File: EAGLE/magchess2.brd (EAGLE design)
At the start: 49.5 x 40.6 mm, 14 parts

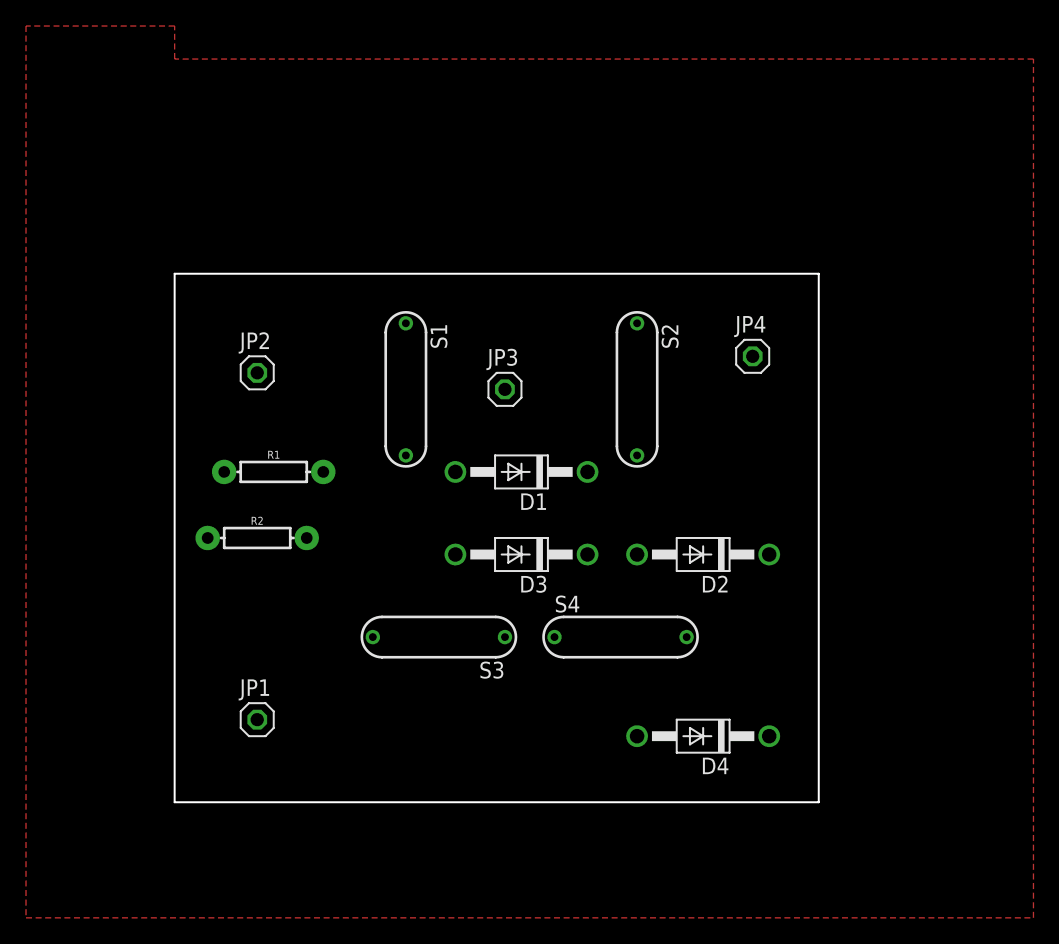
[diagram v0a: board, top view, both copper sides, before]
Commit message: figured out how to work around relaly small garbage
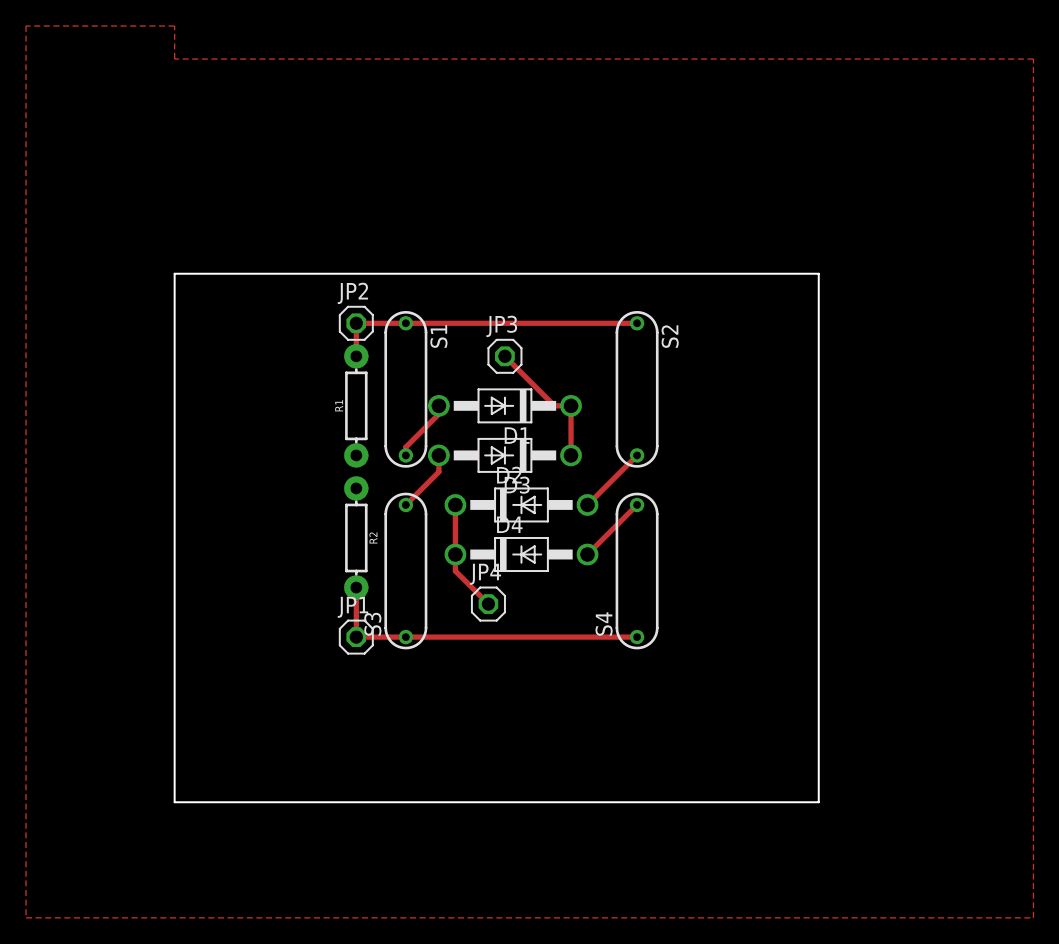
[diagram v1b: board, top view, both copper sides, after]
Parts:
- moved JP4 27.9 mm to (41.9, 29.2)
- moved D4 19.8 mm to (44.5, 33.0), turned to 0 degrees
- moved D2 14.5 mm to (44.5, 36.8), turned to 0 degrees
- moved JP1 9.92 mm to (31.8, 26.7)
- moved JP2 8.52 mm to (31.8, 50.8)
- moved R1 8.13 mm to (31.8, 44.5), turned to 90 degrees
- moved D3 7.73 mm to (43.2, 40.6)
- moved R2 7.62 mm to (31.8, 34.3), turned to 270 degrees
- moved S3 5.68 mm to (35.6, 31.8), turned to 90 degrees
- moved D1 5.24 mm to (43.2, 44.5)
- moved S4 5.24 mm to (53.3, 31.8), turned to 90 degrees
- moved JP3 2.54 mm to (43.2, 48.3)
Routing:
- net N$2: track 0.00 -> 25.4 mm
- net N$1: track 0.00 -> 24.1 mm
- net N$8: track 0.00 -> 10.5 mm
- net N$7: track 0.00 -> 8.67 mm
- net N$6: track 0.00 -> 5.39 mm
- net N$5: track 0.00 -> 5.39 mm
- net N$4: track 0.00 -> 4.86 mm
- net N$3: track 0.00 -> 4.86 mm
